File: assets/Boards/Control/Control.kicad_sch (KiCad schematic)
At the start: 7 parts, among them J3 MAIN_BOARD, J5 MIC, SW1 SW_Push_Dual

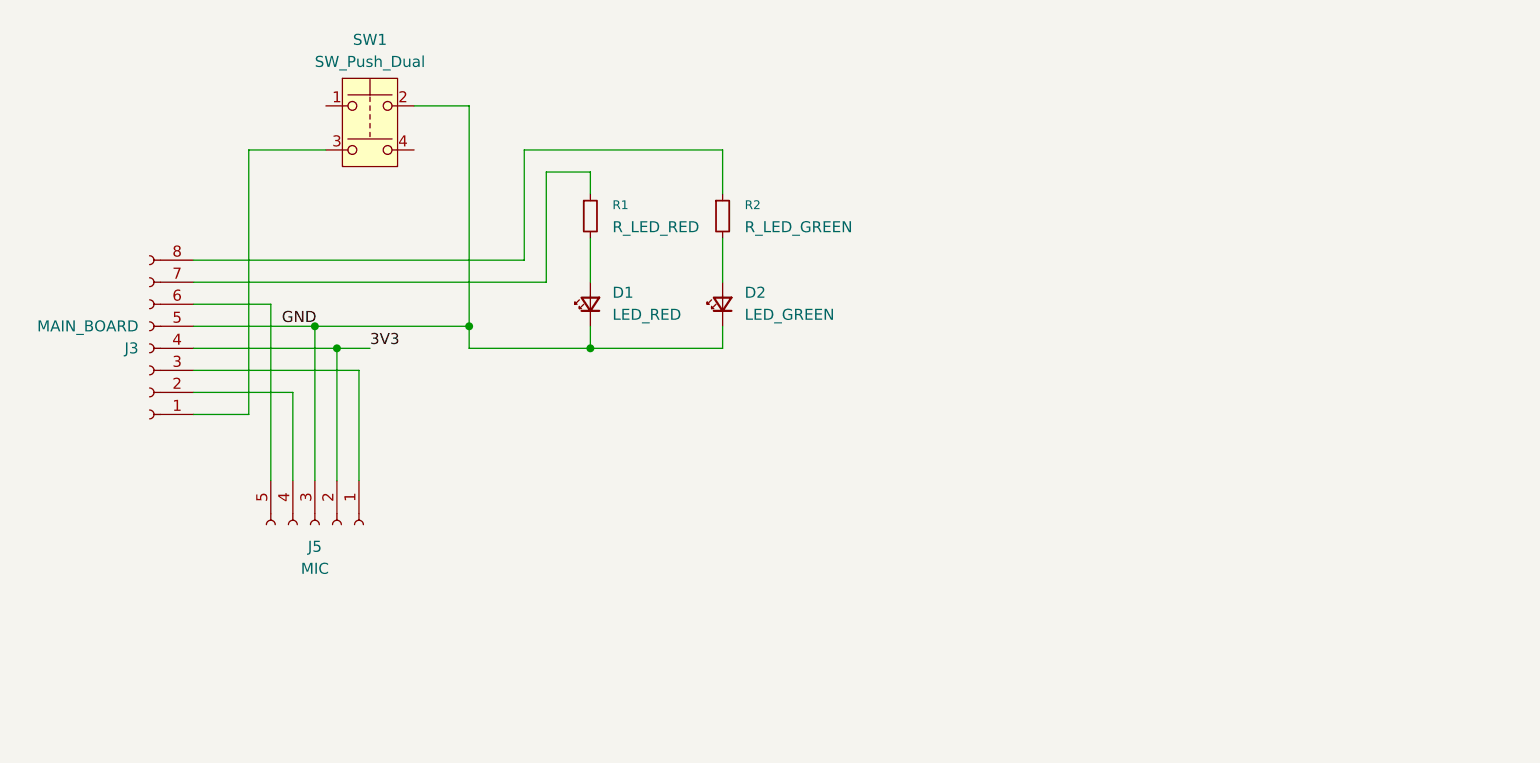
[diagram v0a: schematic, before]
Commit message: Reworked boards.
Added LDO for the mic. Changed layout of the main board to move the cap out of the way. Added ground and power plane. Added R33's for the signal lines of the mic.
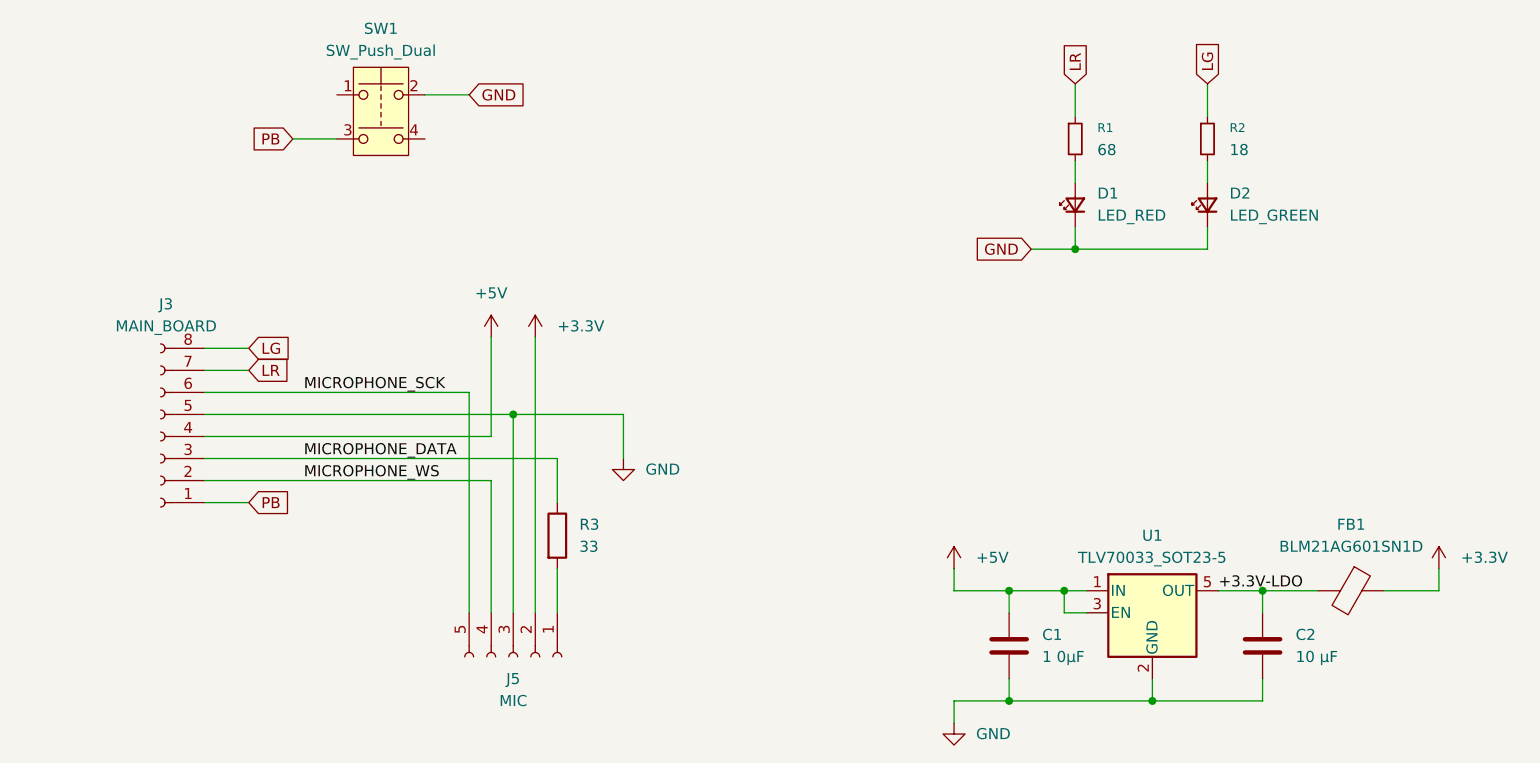
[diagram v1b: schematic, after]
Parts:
- added C1: 1 0µF, Capacitor_SMD:C_0805_2012Metric_Pad1.18x1.45mm_HandSolder, symbol Device:C
- added C2: 10 µF, Capacitor_SMD:C_0805_2012Metric_Pad1.18x1.45mm_HandSolder, symbol Device:C
- added FB1: BLM21AG601SN1D, Inductor_SMD:L_0805_2012Metric_Pad1.15x1.40mm_HandSolder, symbol Device:FerriteBead
- added R3: 33, Resistor_SMD:R_0805_2012Metric_Pad1.20x1.40mm_HandSolder, symbol Device:R
- added U1: TLV70033_SOT23-5, Package_TO_SOT_SMD:SOT-23-5, symbol Regulator_Linear:TLV70033_SOT23-5
- R1: value R_LED_RED -> 68
- R2: value R_LED_GREEN -> 18
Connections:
- net GND: now also C1.1, C2.2, U1.2 (GND)
- net at J5.1 (Pin_1): now also R3.2; no longer J3.3 (Pin_3)
- net MICROPHONE_WS: now reaches J3.2 (Pin_2), J5.4 (Pin_4)
- net MICROPHONE_SCK: now reaches J3.6 (Pin_6), J5.5 (Pin_5)
- net PB: now reaches J3.1 (Pin_1), SW1.3
- net LR: now reaches J3.7 (Pin_7), R1.1
- net LG: now reaches J3.8 (Pin_8), R2.1
- net 3V3 renamed +3.3V
- net +3.3V: now also FB1.1; no longer J3.4 (Pin_4)
- new net +3.3V-LDO: C2.1, FB1.2, U1.5 (OUT)
- new net +5V: C1.2, J3.4 (Pin_4), U1.1 (IN), U1.3 (EN)
- new net MICROPHONE_DATA: J3.3 (Pin_3), R3.1
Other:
- moved on the sheet: D1, D2, J3, J5, R1, R2, SW1

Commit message: Fixed ERC errors. Switched to double ground plane instead of ground and power plane. Switched to 1uF caps for the LDO conforming to the data sheet. Added logo.
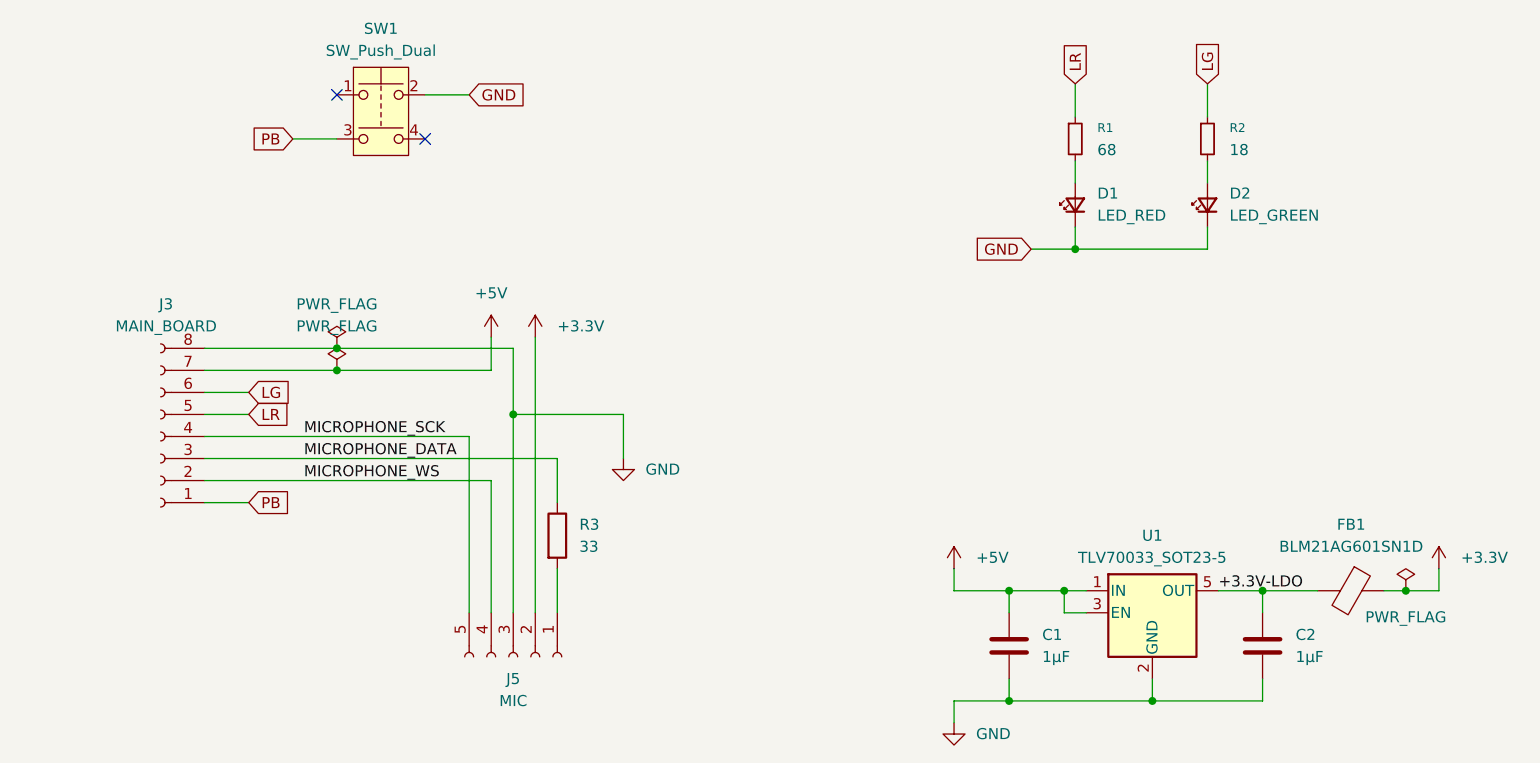
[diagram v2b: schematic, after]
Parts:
- C1: value 1 0µF -> 1µF
- C2: value 10 µF -> 1µF
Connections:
- net +5V: now also J3.7 (Pin_7); no longer J3.4 (Pin_4)
- net GND: now also J3.8 (Pin_8); no longer J3.5 (Pin_5)
- net LG: now also J3.6 (Pin_6); no longer J3.8 (Pin_8)
- net LR: now also J3.5 (Pin_5); no longer J3.7 (Pin_7)
- net MICROPHONE_SCK: now also J3.4 (Pin_4); no longer J3.6 (Pin_6)
- no-connect marks 0 -> 2

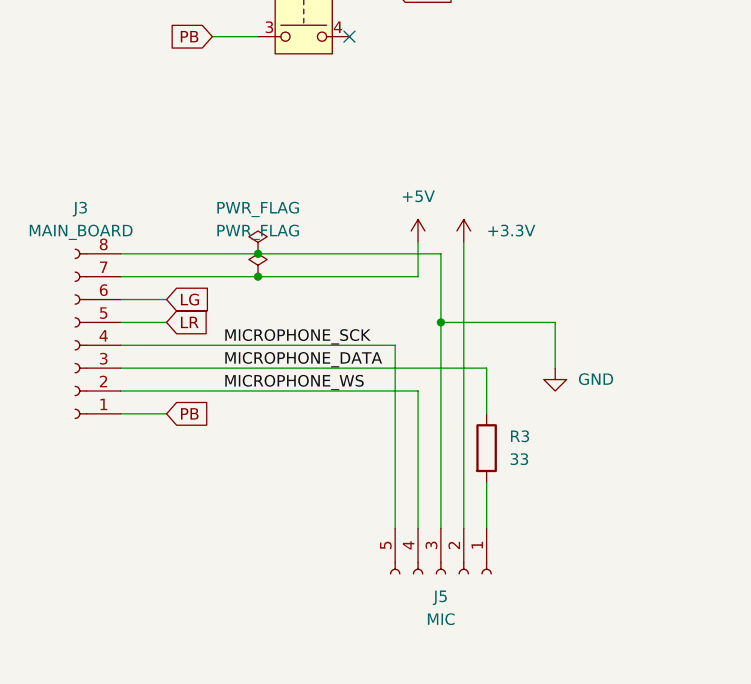
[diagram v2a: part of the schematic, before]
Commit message: Applied suggestions from Rick Hartley.
See https://www.youtube.com/watch?v=ySuUZEjARPY.
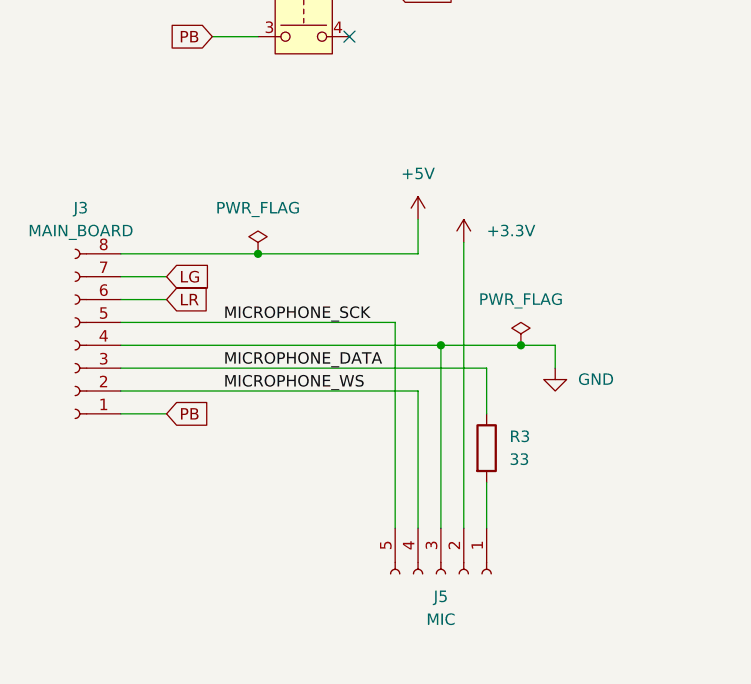
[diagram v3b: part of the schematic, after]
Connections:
- net +5V: now also J3.8 (Pin_8); no longer J3.7 (Pin_7)
- net GND: now also J3.4 (Pin_4); no longer J3.8 (Pin_8)
- net LG: now also J3.7 (Pin_7); no longer J3.6 (Pin_6)
- net LR: now also J3.6 (Pin_6); no longer J3.5 (Pin_5)
- net MICROPHONE_SCK: now also J3.5 (Pin_5); no longer J3.4 (Pin_4)

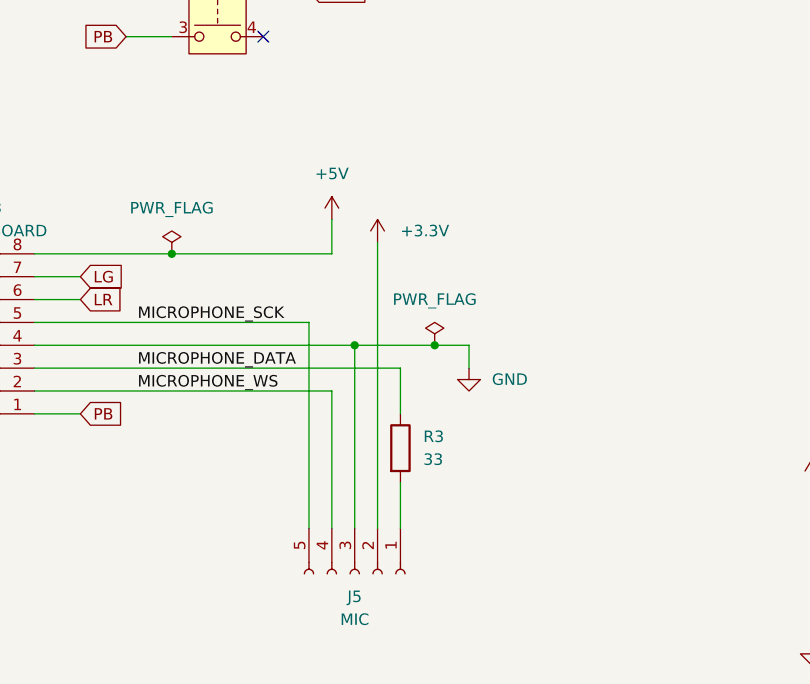
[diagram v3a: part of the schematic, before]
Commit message: Applied suggestions from people from the KiCad forum.
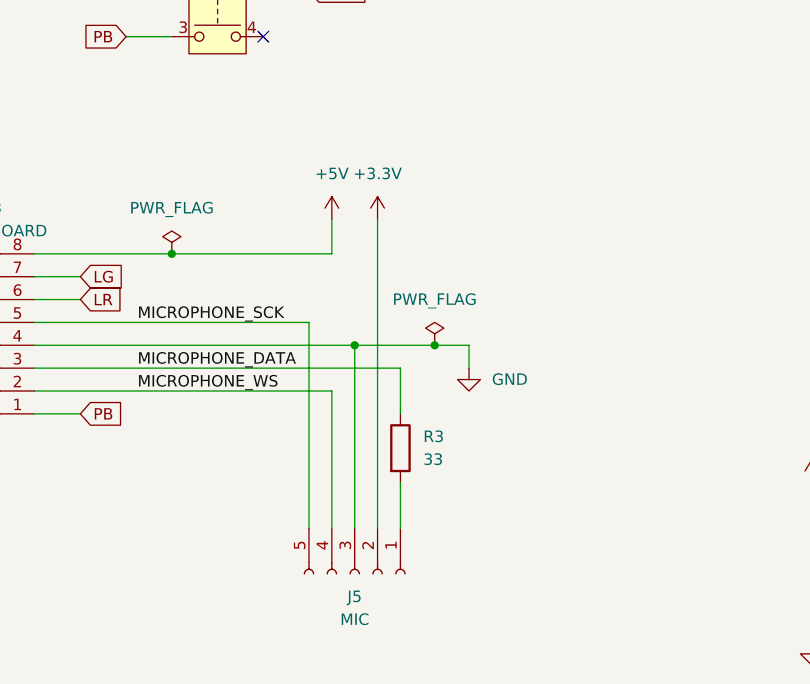
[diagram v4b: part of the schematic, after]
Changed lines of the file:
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@@
 	(wire
 		(pts
-			(xy 128.27 87.63) (xy 128.27 119.38)
+			(xy 128.27 85.09) (xy 128.27 119.38)
 		)
 		(stroke
@@
 	(symbol
 		(lib_id "power:+3.3V")
-		(at 128.27 87.63 0)
+		(at 128.27 85.09 0)
 		(unit 1)
 		(exclude_from_sim no)
@@
 		(on_board yes)
 		(dnp no)
-		(fields_autoplaced yes)
 		(property "Reference" "#PWR04"
-			(at 128.27 91.44 0)
+			(at 128.27 88.9 0)
 			(effects
 				(font
@@
 		)
 		(property "Value" "+3.3V"
-			(at 130.81 86.3599 0)
-			(effects
-				(font
-					(size 1.27 1.27)
-				)
-				(justify left)
+			(at 128.27 80.01 0)
+			(effects
+				(font
+					(size 1.27 1.27)
+				)
 			)
 		)
 		(property "Footprint" ""
-			(at 128.27 87.63 0)
+			(at 128.27 85.09 0)
 			(effects
 				(font
@@
 		)
 		(property "Datasheet" ""
-			(at 128.27 87.63 0)
+			(at 128.27 85.09 0)
 			(effects
 				(font
@@
 		)
 		(property "Description" "Power symbol creates a global label with name \"+3.3V\""
-			(at 128.27 87.63 0)
-			(effects
-				(font
+			(at 128.27 85.09 0)
+			(effects
+				(font
